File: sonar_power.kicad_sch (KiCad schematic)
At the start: 20 parts, among them U201 TPL810ADJ, U202 TPL810ADJ

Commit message: more work
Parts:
- added C208, C209, C210, C211, C212: 220uF 50V, BR_Passives:CAP-Electrolytic_SMD_D6.3-L6.6-W6.6-LS7.4-FD, symbol BR_Capacitors_Electrolytic:C_Alum_220uF_10V_20%_SMD
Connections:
- net 5V: now also C208.1 (+), C209.1 (+), C210.1 (+), C211.1 (+), C212.1 (+)
- net GND: now also C208.2 (-), C209.2 (-), C210.2 (-), C211.2 (-), C212.2 (-)
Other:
- sheet VTX Boost ports: added none; removed MODE
- moved on the sheet: C202, C203, C204, C205, C206, C207, R203, R204, R205, R206, R207, R208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

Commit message: work
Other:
- moved on the sheet: C201, C202, C203, C204, C205, C206, C207, C208, C209, C210, C211, C212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

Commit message: more work
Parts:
- removed TP201, TP202: TP_SQUARE_TH_500um, BR_Virtual_Parts:TP_SQUARE_TH_1mm, symbol BR_Virtual_Parts:TP_SQUARE_TH_1mm

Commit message: fixing some errors
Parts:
- R206, R207, R208, R209: footprint BR_Passives:C_0402_1005Metric-minimized -> BR_Passives:R_0402_1005Metric-minimized
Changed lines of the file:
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@@
 			)
 		)
-		(property "Footprint" "BR_Passives:C_0402_1005Metric-minimized"
+		(property "Footprint" "BR_Passives:R_0402_1005Metric-minimized"
 			(at 411.48 189.23 0)
 			(hide yes)
@@
 			)
 		)
-		(property "Footprint" "BR_Passives:C_0402_1005Metric-minimized"
+		(property "Footprint" "BR_Passives:R_0402_1005Metric-minimized"
 			(at 411.48 151.13 0)
 			(hide yes)
@@
 			)
 		)
-		(property "Footprint" "BR_Passives:C_0402_1005Metric-minimized"
+		(property "Footprint" "BR_Passives:R_0402_1005Metric-minimized"
 			(at 411.48 181.61 0)
 			(hide yes)
@@
 			)
 		)
-		(property "Footprint" "BR_Passives:C_0402_1005Metric-minimized"
+		(property "Footprint" "BR_Passives:R_0402_1005Metric-minimized"
 			(at 411.48 158.75 0)
 			(hide yes)

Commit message: getting really close to final
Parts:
- U201, U202: JLCPCB Part Num (none) -> C5155199
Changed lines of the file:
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@@
+			)
+		)
+		(property "JLCPCB Part Num" "C5155199"
+			(at 383.54 185.42 0)
+			(hide yes)
+			(show_name no)
+			(do_not_autoplace no)
+			(effects
+				(font
+					(size 1.27 1.27)
+				)
+				(justify left)
 			)
 		)
@@
 			(hide yes)
 			(show_name no)
+			(do_not_autoplace no)
+			(effects
+				(font
+					(size 1.27 1.27)
+				)
+				(justify left)
+			)
+		)
+		(property "JLCPCB Part Num" "C5155199"
+			(at 383.54 154.94 0)
+			(hide yes)
+			(show_name no)

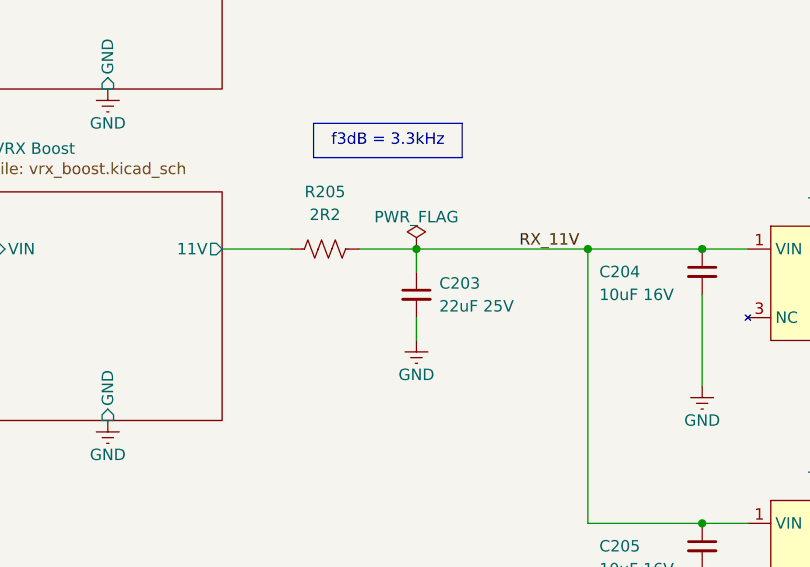
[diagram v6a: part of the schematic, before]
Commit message: made outline 1mm smaller in all directions
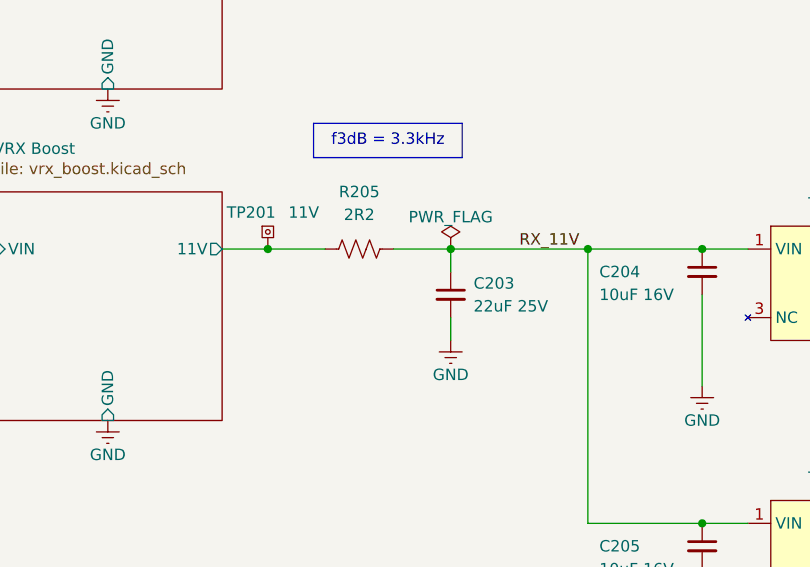
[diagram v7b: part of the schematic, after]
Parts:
- added TP201: 11V, BR_Virtual_Parts:TP_SQUARE_TH_2mm, symbol BR_Virtual_Parts:TP_SQUARE_TH_2mm
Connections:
- net VRX Boost/11V: now also TP201.1
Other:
- moved on the sheet: C203, R205

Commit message: some final changes to rx stage
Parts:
- C208, C209, C210, C211, C212: value 220uF 50V -> 220uF 10V
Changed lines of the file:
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@@
 			)
 		)
-		(property "Value" "220uF 50V"
-			(at 237.744 154.686 0)
+		(property "Value" "220uF 10V"
+			(at 238.506 154.178 0)
 			(show_name no)
 			(do_not_autoplace no)
@@
 		)
 		(property "Description" "220uF 10V 20% Electrolytic Capacitor SMD D6.3xL7.7mm"
-			(at 237.49 81.28 0)
+			(at 237.49 88.9 0)
 			(hide yes)
 			(show_name no)
@@
 		)
 		(property "Manufacturer" "ROQANG"
-			(at 237.49 83.82 0)
+			(at 237.49 81.28 0)
 			(hide yes)
 			(show_name no)
@@
 		)
 		(property "Manufacturer Part Num" "RVT1A221M0607"
-			(at 237.49 86.36 0)
+			(at 237.49 83.82 0)
 			(hide yes)
 			(show_name no)
@@
 		)
 		(property "BRE Number" "BRE-001440"
-			(at 237.49 88.9 0)
+			(at 237.49 86.36 0)
 			(hide yes)
 			(show_name no)
@@
 			)
 		)
-		(property "Value" "220uF 50V"
-			(at 225.044 154.686 0)
+		(property "Value" "220uF 10V"
+			(at 225.806 154.178 0)
 			(show_name no)
 			(do_not_autoplace no)
@@
 		)
 		(property "Description" "220uF 10V 20% Electrolytic Capacitor SMD D6.3xL7.7mm"
-			(at 224.79 81.28 0)
+			(at 224.79 88.9 0)
 			(hide yes)
 			(show_name no)
@@
 		)
 		(property "Manufacturer" "ROQANG"
-			(at 224.79 83.82 0)
+			(at 224.79 81.28 0)
 			(hide yes)
 			(show_name no)
@@
 		)
 		(property "Manufacturer Part Num" "RVT1A221M0607"
-			(at 224.79 86.36 0)
+			(at 224.79 83.82 0)
 			(hide yes)
 			(show_name no)
@@
 		)
 		(property "BRE Number" "BRE-001440"
-			(at 224.79 88.9 0)
+			(at 224.79 86.36 0)
 			(hide yes)
 			(show_name no)
@@
 			)
 		)
-		(property "Value" "220uF 50V"
-			(at 250.444 154.686 0)
+		(property "Value" "220uF 10V"
+			(at 251.206 154.178 0)
 			(show_name no)
 			(do_not_autoplace no)
@@
 		)
 		(property "Description" "220uF 10V 20% Electrolytic Capacitor SMD D6.3xL7.7mm"
-			(at 250.19 81.28 0)
+			(at 250.19 88.9 0)
 			(hide yes)
 			(show_name no)
@@
 		)
 		(property "Manufacturer" "ROQANG"
-			(at 250.19 83.82 0)
+			(at 250.19 81.28 0)
 			(hide yes)
 			(show_name no)
@@
 		)
 		(property "Manufacturer Part Num" "RVT1A221M0607"
-			(at 250.19 86.36 0)
+			(at 250.19 83.82 0)
 			(hide yes)
 			(show_name no)
@@
 		)
 		(property "BRE Number" "BRE-001440"
-			(at 250.19 88.9 0)
+			(at 250.19 86.36 0)
 			(hide yes)
 			(show_name no)
@@
 			)
 		)
-		(property "Value" "220uF 50V"
-			(at 263.144 154.686 0)
+		(property "Value" "220uF 10V"
+			(at 263.906 154.178 0)
 			(show_name no)
 			(do_not_autoplace no)
@@
 		)
 		(property "Description" "220uF 10V 20% Electrolytic Capacitor SMD D6.3xL7.7mm"
-			(at 262.89 81.28 0)
+			(at 262.89 88.9 0)
 			(hide yes)
 			(show_name no)
@@
 		)
 		(property "Manufacturer" "ROQANG"
-			(at 262.89 83.82 0)
+			(at 262.89 81.28 0)
 			(hide yes)
 			(show_name no)
@@
 		)
 		(property "Manufacturer Part Num" "RVT1A221M0607"
-			(at 262.89 86.36 0)
+			(at 262.89 83.82 0)
 			(hide yes)
 			(show_name no)
@@
 		)
 		(property "BRE Number" "BRE-001440"
-			(at 262.89 88.9 0)
+			(at 262.89 86.36 0)
 			(hide yes)
 			(show_name no)
@@
 			)
 		)
-		(property "Value" "220uF 50V"
-			(at 275.844 154.686 0)
+		(property "Value" "220uF 10V"
+			(at 276.606 154.178 0)
 			(show_name no)
 			(do_not_autoplace no)
@@
 		)
 		(property "Description" "220uF 10V 20% Electrolytic Capacitor SMD D6.3xL7.7mm"
-			(at 275.59 81.28 0)
+			(at 275.59 88.9 0)
 			(hide yes)
 			(show_name no)
@@
 		)
 		(property "Manufacturer" "ROQANG"
-			(at 275.59 83.82 0)
+			(at 275.59 81.28 0)
 			(hide yes)
 			(show_name no)
@@
 		)
 		(property "Manufacturer Part Num" "RVT1A221M0607"
-			(at 275.59 86.36 0)
+			(at 275.59 83.82 0)
 			(hide yes)
 			(show_name no)
@@
 		)
 		(property "BRE Number" "BRE-001440"
-			(at 275.59 88.9 0)
+			(at 275.59 86.36 0)
 			(hide yes)
 			(show_name no)
